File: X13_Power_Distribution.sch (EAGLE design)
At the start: 44 parts, among them Q1 IRF1018EPBF, Q2 SSM3K341R, Q3 IRF1018EPBF, Q4 IRF1018EPBF, Q5 SSM3K341R, Q6 SSM3K341R, U1 LM74610, U2 LM74610, U3 LM5050, U4 LM5050

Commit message: playing with 3d package generator in eagle
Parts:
- Q1, Q3, Q4: device Reverse_Voltage_NMOS:IRF1018EPBF -> Dist_Reverse_Voltage_NMOS:IRF1018EPBF
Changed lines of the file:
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@@
 <setting verticaltext="up"/>
 </settings>
-<grid distance="0.05" unitdist="inch" unit="inch" style="lines" multiple="1" display="no" altdistance="0.01" altunitdist="inch" altunit="inch"/>
+<grid distance="0.1" unitdist="inch" unit="inch" style="lines" multiple="1" display="no" altdistance="0.01" altunitdist="inch" altunit="inch"/>
 <layers>
 <layer number="1" name="Top" color="4" fill="1" visible="no" active="no"/>
@@
 <attribute name="SPICEPREFIX" value="R"/>
 </part>
-<part name="Q1" library="Reverse_Voltage_NMOS" deviceset="IRF1018EPBF" device=""/>
+<part name="Q1" library="Dist_Reverse_Voltage_NMOS" deviceset="IRF1018EPBF" device="" package3d_urn="urn:adsk.eagle:package:25914649/1"/>
 <part name="R1" library="SparkFun-Resistors" library_urn="urn:adsk.eagle:library:532" deviceset="RESISTOR" device="0603" package3d_urn="urn:adsk.eagle:package:39650/1" value="1M"/>
 <part name="D1" library="SparkFun-DiscreteSemi" library_urn="urn:adsk.eagle:library:514" deviceset="DIODE-ZENER" device="-BZT52C3V6S" package3d_urn="urn:adsk.eagle:package:38441/1" value="15V"/>
@@
 <part name="U1" library="Dist_OR_Controller" deviceset="DIST_OR_DIODE" device="DGK0008A_M" value="LM74610"/>
 <part name="U2" library="Dist_OR_Controller" deviceset="DIST_OR_DIODE" device="DGK0008A_M" value="LM74610"/>
-<part name="Q3" library="Reverse_Voltage_NMOS" deviceset="IRF1018EPBF" device=""/>
-<part name="Q4" library="Reverse_Voltage_NMOS" deviceset="IRF1018EPBF" device=""/>
+<part name="Q3" library="Dist_Reverse_Voltage_NMOS" deviceset="IRF1018EPBF" device="" package3d_urn="urn:adsk.eagle:package:25914649/1"/>
+<part name="Q4" library="Dist_Reverse_Voltage_NMOS" deviceset="IRF1018EPBF" device="" package3d_urn="urn:adsk.eagle:package:25914649/1"/>
 <part name="D4" library="SparkFun-DiscreteSemi" library_urn="urn:adsk.eagle:library:514" deviceset="DIODE-ZENER" device="-BZT52C3V6S" package3d_urn="urn:adsk.eagle:package:38441/1" value="5V"/>
 <part name="Q2" library="SparkFun-DiscreteSemi" library_urn="urn:adsk.eagle:library:514" deviceset="MOSFET-NCH" device="-2N7002PW" package3d_urn="urn:adsk.eagle:package:38456/1" value="SSM3K341R"/>

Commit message: Some more edits
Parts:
- added +12V_A_TEST, +12V_B_TEST, +12V_TEST, +48V_TEST, 12_GND, 48GND_TEST: SSW-101-02-G-S, con-samtec:SSW-101-02-G-S
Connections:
- net +12V: now also +12V_TEST.1
- net +12V_A: now also +12V_A_TEST.1
- net +12V_B: now also +12V_B_TEST.1
- net +48V: now also +48V_TEST.1
- net 12V_GND: now also 12_GND.1
- net 48V_GND: now also 48GND_TEST.1
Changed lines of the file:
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@@
 <part name="BRICK1" library="Brick_Dist_Connector" deviceset="DIST2BRICK" device="VER_D2"/>
 <part name="BRICK2" library="Brick_Dist_Connector" deviceset="DIST2BRICK" device="VER_D2"/>
+<part name="+48V_TEST" library="con-samtec" library_urn="urn:adsk.eagle:library:184" deviceset="SSW-101-02-G-S" device=""/>
+<part name="48GND_TEST" library="con-samtec" library_urn="urn:adsk.eagle:library:184" deviceset="SSW-101-02-G-S" device=""/>
+<part name="+12V_A_TEST" library="con-samtec" library_urn="urn:adsk.eagle:library:184" deviceset="SSW-101-02-G-S" device=""/>
+<part name="12_GND" library="con-samtec" library_urn="urn:adsk.eagle:library:184" deviceset="SSW-101-02-G-S" device=""/>
+<part name="+12V_B_TEST" library="con-samtec" library_urn="urn:adsk.eagle:library:184" deviceset="SSW-101-02-G-S" device=""/>
+<part name="+12V_TEST" library="con-samtec" library_urn="urn:adsk.eagle:library:184" deviceset="SSW-101-02-G-S" device=""/>
 </parts>
 <sheets>
@@
 <instance part="BRICK2" gate="G$1" x="38.1" y="63.5" smashed="yes">
 <attribute name="NAME" x="38.608" y="72.136" size="1.778" layer="95"/>
+</instance>
+<instance part="+48V_TEST" gate="-1" x="312.42" y="111.76" smashed="yes">
+<attribute name="VALUE" x="309.88" y="114.3" size="1.778" layer="96"/>
+<attribute name="NAME" x="309.372" y="112.522" size="1.524" layer="95" rot="R180"/>
+</instance>
+<instance part="48GND_TEST" gate="-1" x="312.42" y="106.68" smashed="yes">
+<attribute name="VALUE" x="309.88" y="109.22" size="1.778" layer="96"/>
+<attribute name="NAME" x="309.372" y="107.442" size="1.524" layer="95" rot="R180"/>
+</instance>
+<instance part="+12V_A_TEST" gate="-1" x="312.42" y="81.28" smashed="yes">
+<attribute name="VALUE" x="309.88" y="83.82" size="1.778" layer="96"/>
+<attribute name="NAME" x="309.372" y="82.042" size="1.524" layer="95" rot="R180"/>
+</instance>
+<instance part="12_GND" gate="-1" x="312.42" y="76.2" smashed="yes">
+<attribute name="VALUE" x="309.88" y="78.74" size="1.778" layer="96"/>
+<attribute name="NAME" x="309.372" y="76.962" size="1.524" layer="95" rot="R180"/>
+</instance>
+<instance part="+12V_B_TEST" gate="-1" x="312.42" y="71.12" smashed="yes">
+<attribute name="VALUE" x="309.88" y="73.66" size="1.778" layer="96"/>
+<attribute name="NAME" x="309.372" y="71.882" size="1.524" layer="95" rot="R180"/>
+</instance>
+<instance part="+12V_TEST" gate="-1" x="312.42" y="66.04" smashed="yes">
+<attribute name="VALUE" x="309.88" y="68.58" size="1.778" layer="96"/>
+<attribute name="NAME" x="309.372" y="66.802" size="1.524" layer="95" rot="R180"/>
 </instance>
 </instances>
@@
 <label x="299.72" y="160.02" size="0.8128" layer="95" rot="R180" xref="yes"/>
 </segment>
+<segment>
+<pinref part="+12V_TEST" gate="-1" pin="1"/>
+<wire x1="314.96" y1="66.04" x2="317.5" y2="66.04" width="0.1524" layer="91"/>
+<label x="317.5" y="66.04" size="0.8128" layer="95" xref="yes"/>
+</segment>
 </net>
 <net name="+12V_A" class="0">
@@
 <label x="299.72" y="154.94" size="0.8128" layer="95" rot="R180" xref="yes"/>
 </segment>
+<segment>
+<pinref part="+12V_A_TEST" gate="-1" pin="1"/>
+<wire x1="314.96" y1="81.28" x2="317.5" y2="81.28" width="0.1524" layer="91"/>
+<label x="317.5" y="81.28" size="0.8128" layer="95" xref="yes"/>
+</segment>
 </net>
 <net name="+12V_B" class="0">
@@
 <wire x1="302.26" y1="129.54" x2="299.72" y2="129.54" width="0.1524" layer="91"/>
 <label x="299.72" y="129.54" size="0.8128" layer="95" rot="R180" xref="yes"/>
+</segment>
+<segment>
+<pinref part="+12V_B_TEST" gate="-1" pin="1"/>
+<wire x1="314.96" y1="71.12" x2="317.5" y2="71.12" width="0.1524" layer="91"/>
+<label x="317.5" y="71.12" size="0.8128" layer="95" xref="yes"/>
 </segment>
 </net>
@@
 <wire x1="184.15" y1="154.94" x2="168.91" y2="154.94" width="0.1524" layer="91"/>
 <junction x="168.91" y="154.94"/>
-<wire x1="184.15" y1="154.94" x2="189.23" y2="154.94" width="0.1524" layer="91"/>
+<wire x1="184.15" y1="154.94" x2="186.182" y2="154.94" width="0.1524" layer="91"/>
 <junction x="184.15" y="154.94"/>
-<label x="189.23" y="154.94" size="1.778" layer="95" xref="yes"/>
+<label x="186.182" y="154.94" size="1.778" layer="95" rot="R90" xref="yes"/>
 <pinref part="D4" gate="G$1" pin="C"/>
 <wire x1="168.91" y1="151.13" x2="168.91" y2="154.94" width="0.1524" layer="91"/>
@@
 <pinref part="CONVERSION" gate="G$1" pin="VIN+"/>
 </segment>
+<segment>
+<pinref part="+48V_TEST" gate="-1" pin="1"/>
+<wire x1="314.96" y1="111.76" x2="317.5" y2="111.76" width="0.1524" layer="91"/>
+<label x="317.5" y="111.76" size="0.8128" layer="95" xref="yes"/>
+</segment>
 </net>
 <net name="48V_GND" class="0">
@@
 <label x="31.75" y="19.05" size="1.778" layer="95" rot="R180" xref="yes"/>
 <pinref part="CONVERSION" gate="G$1" pin="VIN-"/>
+</segment>
+<segment>
+<pinref part="48GND_TEST" gate="-1" pin="1"/>
+<wire x1="314.96" y1="106.68" x2="317.5" y2="106.68" width="0.1524" layer="91"/>
+<label x="317.5" y="106.68" size="0.8128" layer="95" xref="yes"/>
 </segment>
 </net>
@@
 <label x="340.36" y="157.48" size="0.8128" layer="95" xref="yes"/>
 </segment>
-</net>
+<segment>
+<pinref part="12_GND" gate="-1" pin="1"/>
+<wire x1="314.96" y1="76.2" x2="317.5" y2="76.2" width="0.1524" layer="91"/>
+<label x="317.5" y="76.2" size="0.8128" layer="95" xref="yes"/>
+<wire x1="314.96" y1="76.2" x2="317.5" y2="76.2" width="0.1524" layer="91"/>
+</segment>
+</net>

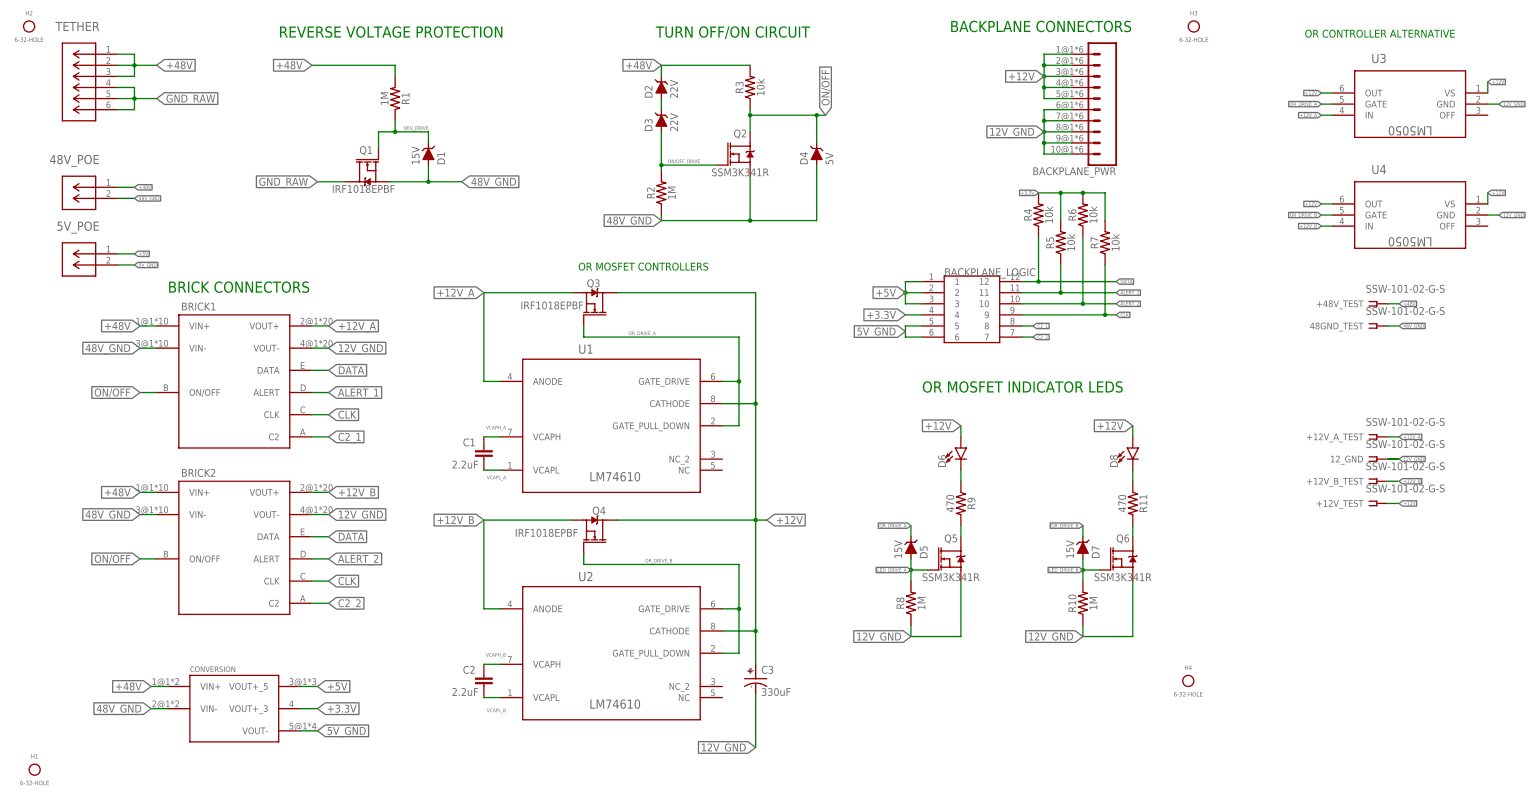
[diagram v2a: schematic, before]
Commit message: Lower on/off threshold, remove old unused or-ing controller, try new 12V on LED circuit
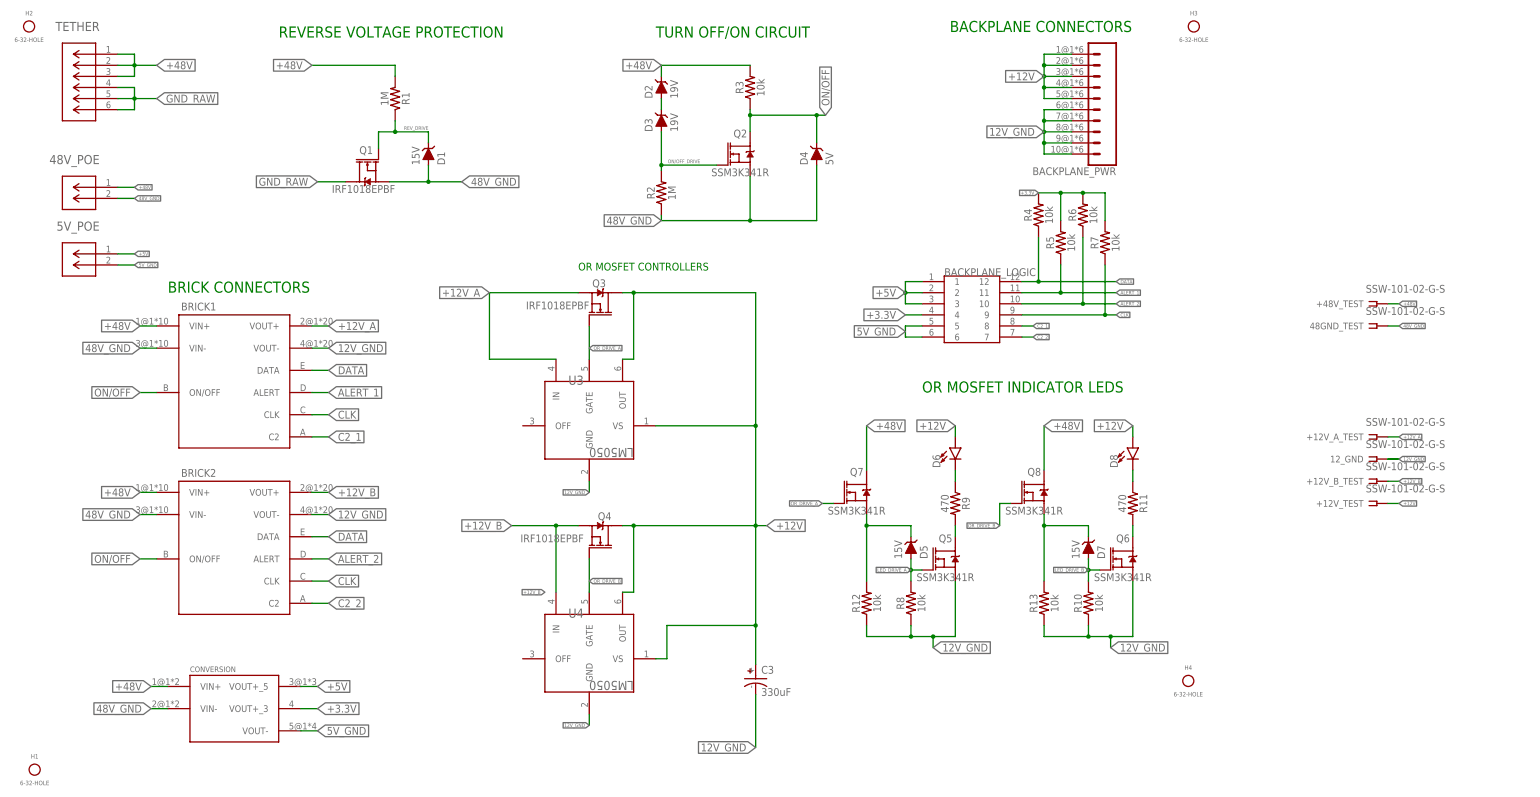
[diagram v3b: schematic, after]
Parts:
- removed C1, C2: 2.2uF, SparkFun-Capacitors:0.1UF-0603-100V-10%
- removed U1, U2: LM74610, Dist_OR_Controller:DIST_OR_DIODEDGK0008A_M
- added Q7, Q8: SSM3K341R, SparkFun-DiscreteSemi:MOSFET-NCH-2N7002PW
- added R12, R13: 10k, SparkFun-Resistors:RESISTOR0603
- D2, D3: value 22V -> 19V
- R10, R8: value 1M -> 10k
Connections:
- removed net VCAPH_A: C1.1, U1.VCAPH
- removed net VCAPH_B: C2.1, U2.VCAPH
- removed net VCAPL_A: C1.2, U1.VCAPL
- removed net VCAPL_B: C2.2, U2.VCAPL
- new net N$2: D5.C, Q7.S, R12.2
- new net N$3: D7.C, Q8.S, R13.2
- net +12V: no longer U1.CATHODE, U2.CATHODE
- net +12V_A: no longer U1.ANODE
- net +12V_B: no longer U2.ANODE
- net +48V: now also Q7.D, Q8.D
- net 12V_GND: now also R12.1, R13.1
- net OR_DRIVE_A: now also Q7.G; no longer D5.C, U1.GATE_DRIVE, U1.GATE_PULL_DOWN
- net OR_DRIVE_B: now also Q8.G; no longer D7.C, U2.GATE_DRIVE, U2.GATE_PULL_DOWN
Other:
- note removed: "OR CONTROLLER ALTERNATIVE"
- moved on the sheet: D6, D7, Q3, Q4, Q5, R10, R9, U3, U4

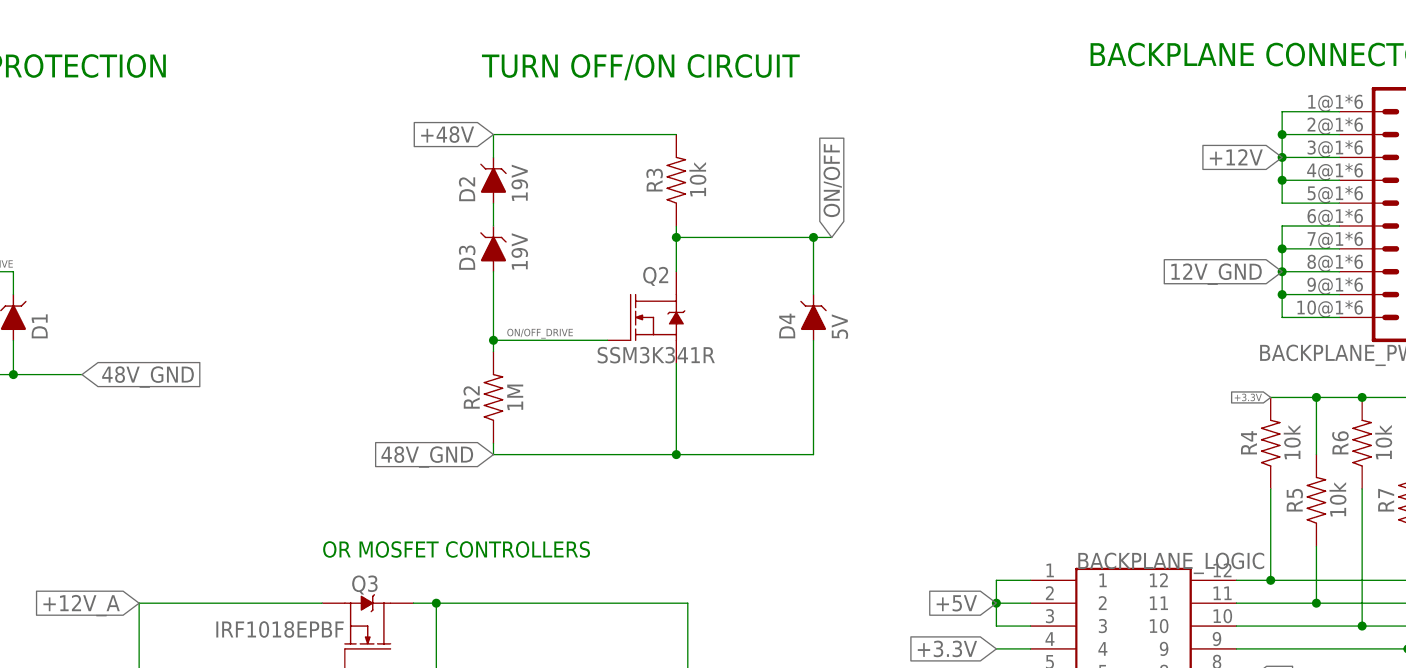
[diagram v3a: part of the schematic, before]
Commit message: Add solder jumper to short on/off and diode to latch voltage
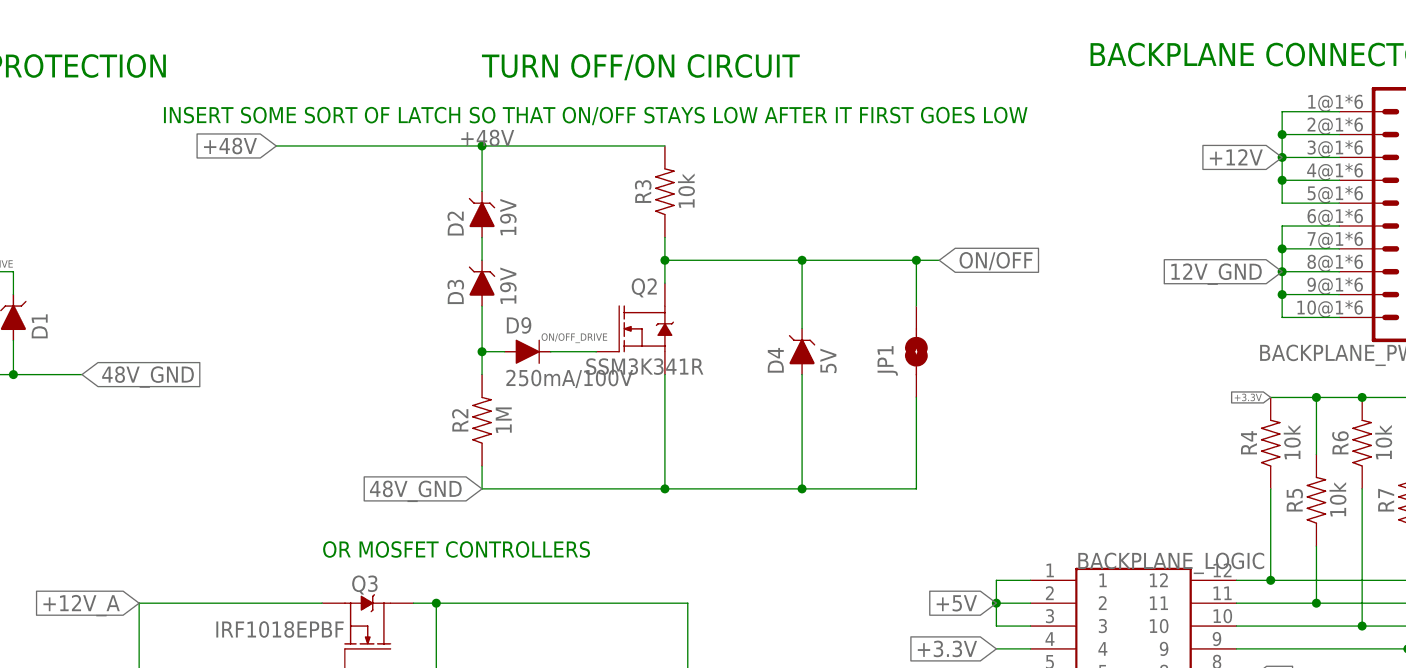
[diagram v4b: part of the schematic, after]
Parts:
- added D9: 250mA/100V, SparkFun-DiscreteSemi:DIODE-BAS16J
- added JP1: JUMPER-SMT_2_NO_SILK, SparkFun-Jumpers:JUMPER-SMT_2_NO_SILK
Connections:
- new net ON_DETECT: D3.A, D9.A, R2.2
- net 48V_GND: now also JP1.1
- net ON/OFF: now also JP1.2
- net ON/OFF_DRIVE: now also D9.C; no longer D3.A, R2.2
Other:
- note added: "INSERT SOME SORT OF LATCH SO THAT ON/OFF STAYS LOW AFTER IT FIRST GOES LOW"
- moved on the sheet: D2, D3, D4, Q2, R2, R3

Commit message: Add diode to on/off to discharge gate when power supply hits 0
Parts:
- added D10: 250mA/100V, SparkFun-DiscreteSemi:DIODE-BAS16J
- added J1: (no value), SparkFun-Connectors:CONN_02
- added J2: (no value), SparkFun-Connectors:CONN_01
- +12V_A_TEST, +12V_B_TEST, +12V_TEST, +48V_TEST, 12_GND, 48GND_TEST: value SSW-101-02-G-S -> (none); device con-samtec:SSW-101-02-G-S -> SparkFun-Connectors:CONN_01
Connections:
- net +48V: now also D10.C
- net CLK: now also J1.1
- net DATA: now also J1.2
- net ON/OFF: now also J2.1
- net ON/OFF_DRIVE: now also D10.A
